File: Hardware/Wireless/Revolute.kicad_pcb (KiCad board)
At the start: 4 copper layers, 19.8 x 20 mm, 60 parts, among them U1 BQ27441-G1, U10 Button, U2 nrf52833_qfn40, U3 AS5600, U4 AP2112K-3.3, U5 BQ24075RGT, U6 Button, U8 Button, U9 Button, X1 32.768 kHz, X2 32MHZ

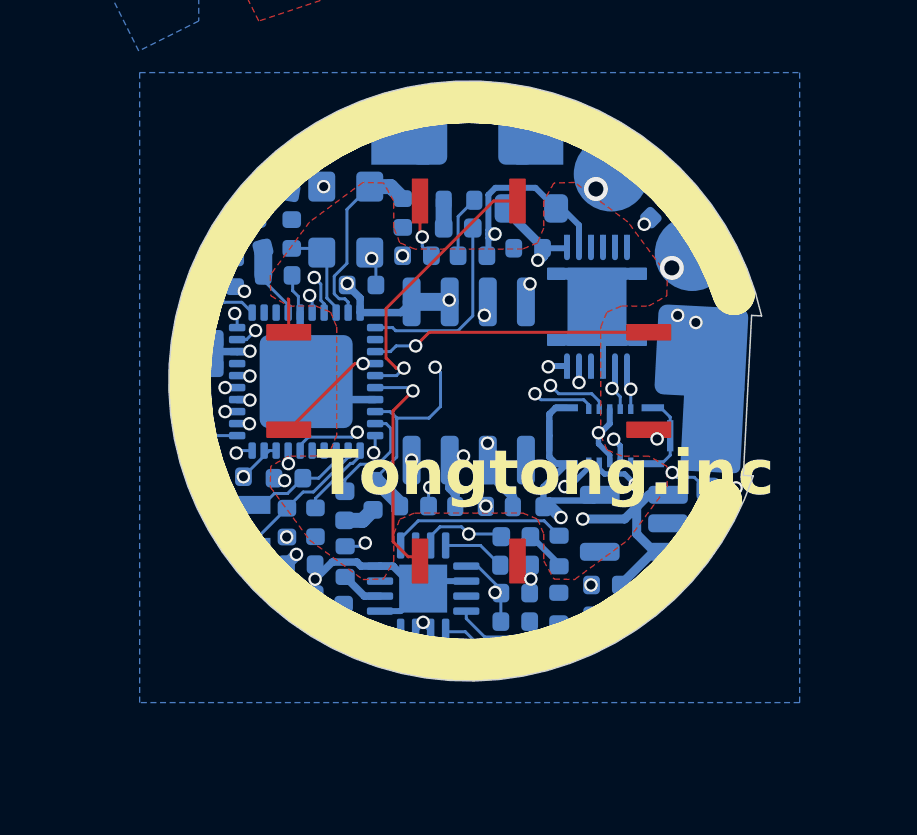
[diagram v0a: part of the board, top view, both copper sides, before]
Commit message: added testing pads to depricate fpc connector
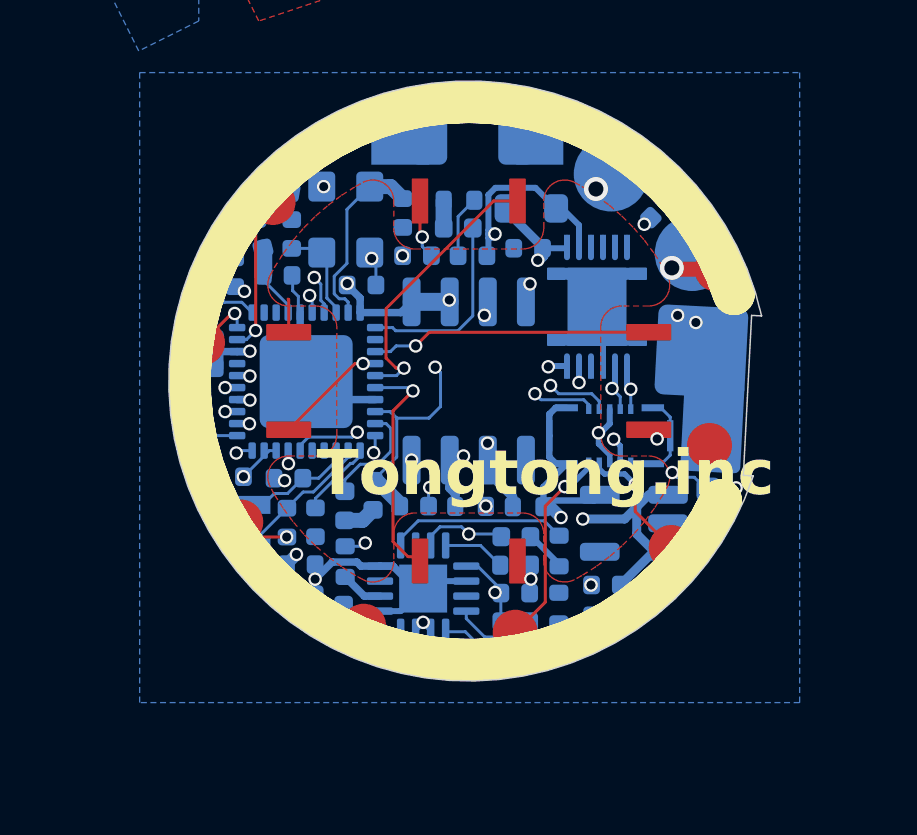
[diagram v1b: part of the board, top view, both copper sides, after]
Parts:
- added ?: , , F.Cu at (179.0, 97.2)
- added ?: , , F.Cu at (172.6, 103.4)
- added ?: , , F.Cu at (164.5, 89.0)
- added ?: , , F.Cu at (179.3, 91.3)
- added ?: , , F.Cu at (163.4, 99.7)
- added ?: , , F.Cu at (177.8, 100.5)
- added ?: , , F.Cu at (162.1, 93.7)
- added ?: , , F.Cu at (167.5, 103.2)
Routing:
- net D-: track 13.3 -> 18.9 mm
- net swd: track 13.8 -> 18.3 mm
- net D+: track 16.9 -> 19.4 mm
- net GND: track 35.4 -> 37.1 mm
- net VBUS: track 35.3 -> 36.8 mm
- net swc: track 15.5 -> 17.0 mm
- net VDD_nRF: track 22.3 -> 23.7 mm, vias 8 -> 9

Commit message: added ID column
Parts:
- AE1: value Antenna -> 2.4G ANT
- C12: value 0.47uF -> 470nF
- U7: value ~ -> BK13C06-10DS

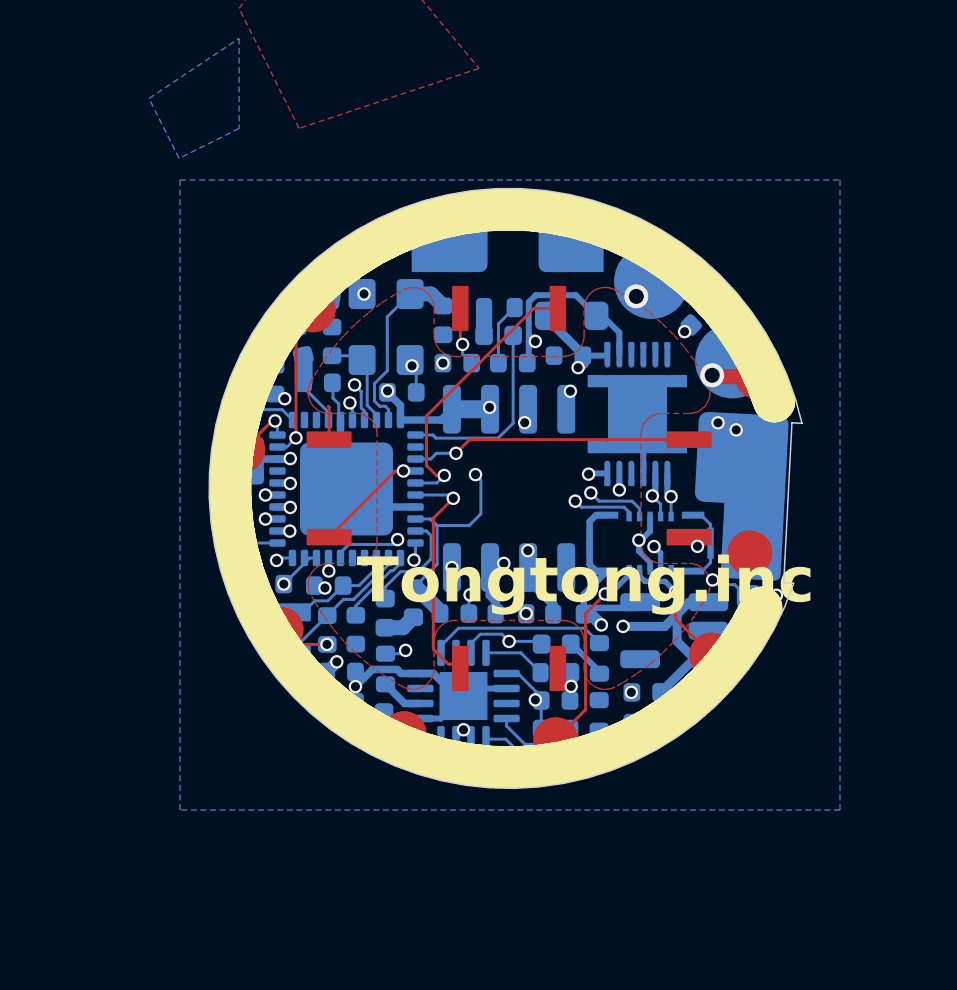
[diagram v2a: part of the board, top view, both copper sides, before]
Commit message: migrated components to 0201
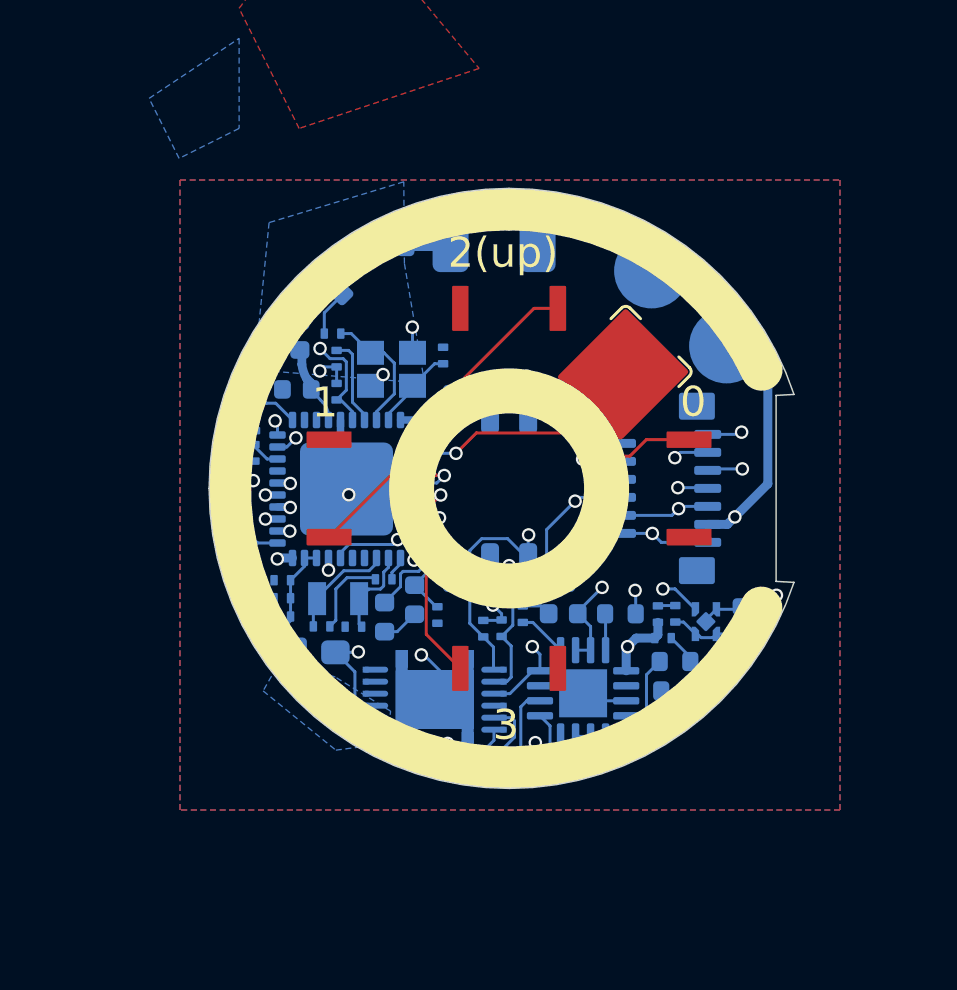
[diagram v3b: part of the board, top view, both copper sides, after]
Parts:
- removed ? (x11): , 
- removed C10: 100nF, Capacitor_SMD:C_0402_1005Metric
- added R10: 0Ω, Library:Resistor-0201, B.Cu at (171.1, 104.4)
- added REF**: Battery Base, Library:Battery Base, F.Cu at (171.0, 95.0)
- C1, C11, C12, C13, C14, C16, C17, C18, C2, C20, C21, C22, C23, C24, C3, C4, C5, C6, C7, C8, C9: footprint Capacitor_SMD:C_0402_1005Metric -> Library:Capacitor-0201
- R3: footprint Library:Resistor_0402_1005M-nosilk -> Library:Resistor-0201
- R6, R8: footprint Resistor_SMD:R_0402_1005Metric -> Library:Resistor-0201
- R7: value 10K -> 0Ω; footprint Library:Resistor_0402_1005M-nosilk -> Library:Resistor-0201
- R9: value 180 -> 1.5k; footprint Library:Resistor_0402_1005M-nosilk -> Library:Resistor-0201
- U4: value AP2112K-3.3 -> MIC5504; footprint Package_TO_SOT_SMD:SOT-23-5 -> Library:TDFN-4
- U7: value BK13C06-10DS -> Conn_01x14_Socket; footprint Library:BK13C06-10DS -> Library:FPC
- X2: footprint Library:crystal 32mhz -> Library:Crystal_SMD_2016-4Pin_2.0x1.6mm
- moved C12 16.9 mm to (169.9, 104.3), turned to 180 degrees
- moved R1 14.4 mm to (165.2, 101.3), turned to 90 degrees
- moved C25 13.6 mm to (163.9, 100.7), turned to -90 degrees
- moved C4 13.6 mm to (168.8, 104.2)
- moved R2 12.2 mm to (162.3, 97.9), turned to 90 degrees
- moved U1 11.7 mm to (168.5, 102.0), turned to 180 degrees
- moved D1 10.2 mm to (162.0, 95.4), turned to 90 degrees
- moved R7 6.16 mm to (172.1, 104.3), turned to 0 degrees
- moved C23 5.61 mm to (161.9, 92.8), turned to 90 degrees
- moved C24 5.13 mm to (176.0, 99.2), turned to 90 degrees
- moved C26 4.66 mm to (178.8, 99.4), turned to 90 degrees
- moved TH1 4.59 mm to (176.6, 101.8)
- moved C6 4.14 mm to (176.1, 100.0)
- moved C18 4.03 mm to (165.2, 90.7), turned to 90 degrees
- moved U5 3.99 mm to (173.5, 101.8)
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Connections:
- R7 pad 1: OUT -> GND
- R7 pad 2: Net-(U5-EN1) -> Net-(U5-EN2)
- U4 pad 1: OUT -> VDD_nRF
- U4 pad 4: unconnected-(U4-NC-Pad4) -> OUT
- U4 pad 5: VDD_nRF -> GND
- U5 pad 5: GND -> Net-(U5-EN2)
- U7 pad 1: swd -> swc
- U7 pad 11: VDD_nRF -> VBUS
- U7 pad 12: VDD_nRF -> Batteryin
- U7 pad 13: VDD_nRF -> Batteryin
- U7 pad 14: GND -> unconnected-(U7-Pin_14-Pad14)
- U7 pad 15: GND -> (no net)
- U7 pad 2: swc -> swd
- U7 pad 3: VBUS -> D-
- U7 pad 4: P0.15 -> D+
- U7 pad 5: P0.17 -> RESET
- U7 pad 6: D- -> VDD_nRF
- U7 pad 7: D+ -> P0.17
- U7 pad 8: VBUS -> P0.15
- U7 pad 9: RESET -> GND
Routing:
- net vBAT: track 21.5 -> 2.38 mm
- net Batteryin: track 22.5 -> 9.22 mm, vias 4 -> 3
- net VDD_nRF: track 23.7 -> 13.5 mm, vias 9 -> 7
- net ASOUT: track 9.98 -> 18.8 mm
- net OUT: track 20.5 -> 11.8 mm, vias 3 -> 2
- net VBUS: track 36.8 -> 29.5 mm, vias 4 -> 3
- net swd: track 18.3 -> 12.0 mm
- net GND: track 37.1 -> 31.1 mm, vias 24 -> 14
- net D+: track 19.4 -> 13.8 mm
- net 1.8V: track 8.23 -> 2.70 mm, vias 2 -> 0
- net P0.17: track 21.0 -> 26.3 mm
- net Net-(U5-~{CHG}): track 5.97 -> 1.64 mm
- net Net-(C19-Pad2): track 0.00 -> 3.87 mm
- net Net-(U2-XC2): track 6.26 -> 2.80 mm
- net D-: track 18.9 -> 15.6 mm
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- added copper zone on B.Cu, net vBAT
- added copper zone on In2.Cu, net vBAT
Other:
- board size 19.8 x 20 mm -> 19.5 x 20 mm
- board text added: "0"
- board text added: "1"
- board text added: "2(up)"
- board text added: "3"
- board text added: "Stack up JLC04161H-7628"

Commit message: refined pcb
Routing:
- added copper zone on B.Cu, net VBUS
- added copper zone on B.Cu, net VDD_nRF

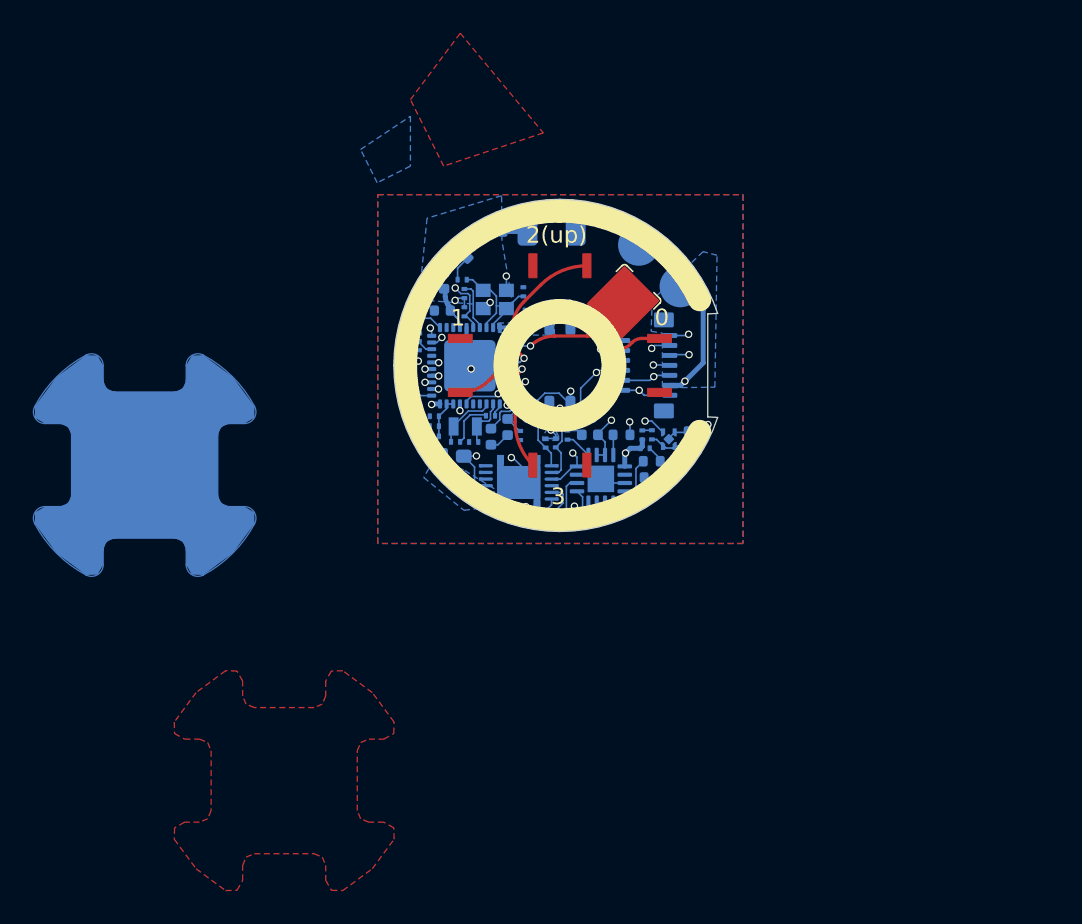
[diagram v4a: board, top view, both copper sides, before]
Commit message: updated pcb 0201 components and flex battery attachment
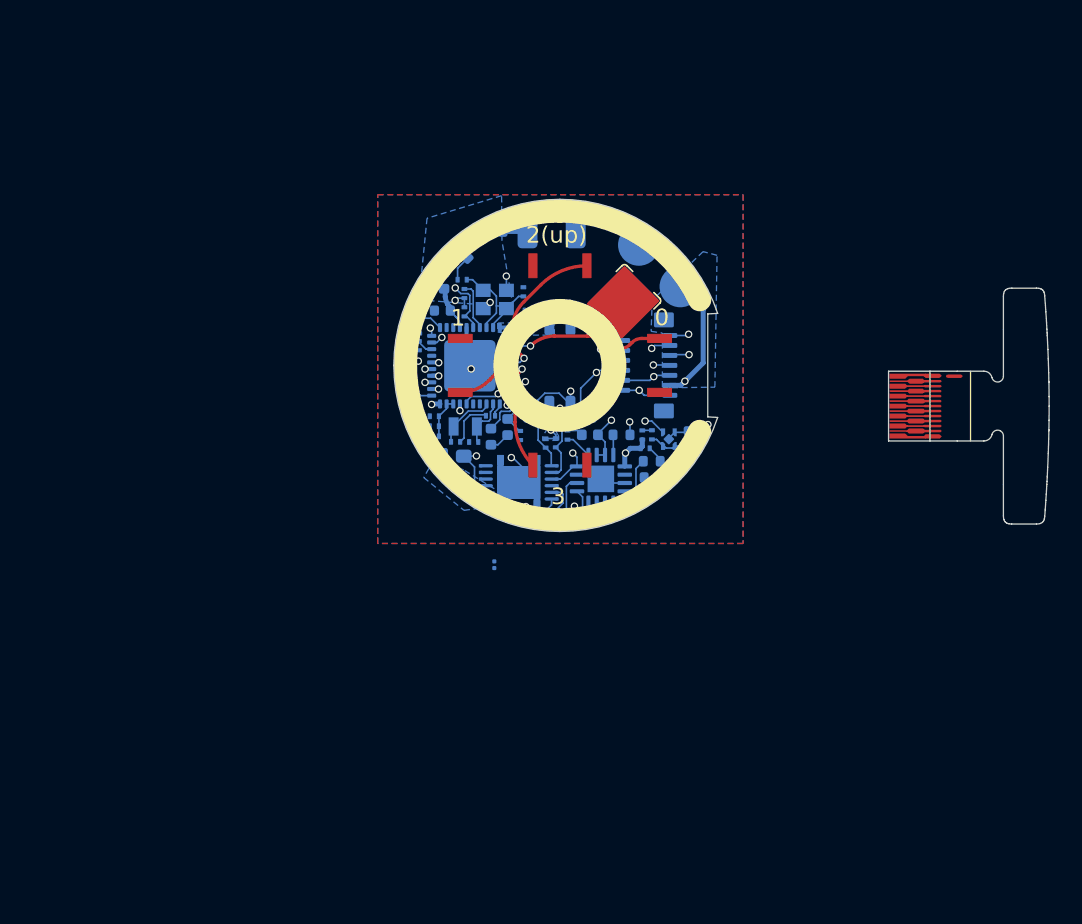
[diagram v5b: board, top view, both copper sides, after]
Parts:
- added REF**: C_01005_0402Metric, Capacitor_SMD:C_01005_0402Metric, B.Cu at (167.1, 107.0)
- added REF**: flex connector, Library:flex connector, B.Cu at (194.7, 95.2)
- moved AE1 0.16 mm to (170.5, 87.0)
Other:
- board size 19.5 x 20 mm -> 39.5 x 20 mm

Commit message: current version
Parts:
- removed the REF** at (167.1, 107.0)
- removed the REF** at (194.7, 95.2)
- AE1: footprint RF_Antenna:Johanson_2450AT18x100 -> Library:Antenna 2450AT42A100
- C15, C19: footprint Capacitor_SMD:C_0402_1005Metric -> Library:Capacitor-0201
- R2: footprint Library:Resistor_0402_1005M-nosilk -> Library:Resistor-0201
- moved L4 3.34 mm to (164.5, 89.1), turned to 30 degrees
- moved C19 2.39 mm to (163.6, 90.0), turned to 130 degrees
- moved AE1 2.29 mm to (168.5, 88.2), turned to 18 degrees
- moved R2 1.21 mm to (162.0, 96.7), turned to 0 degrees
- moved L3 1.20 mm to (163.3, 90.8), turned to 130 degrees
- moved C8 1.14 mm to (162.5, 97.7), turned to 90 degrees
- moved C14 0.46 mm to (162.4, 92.0), turned to 0 degrees
- moved C15 0.32 mm to (164.2, 91.8), turned to 45 degrees
- moved C9 0.08 mm to (165.2, 91.7)
- moved C25 0.07 mm to (164.0, 100.8)
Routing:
- net GND: track 31.1 -> 38.7 mm, vias 14 -> 17
- net Net-(C19-Pad2): track 3.87 -> 1.64 mm
- net OUT: track 11.8 -> 10.5 mm
- net Net-(U2-DEC4): track 15.7 -> 17.0 mm
- net P0.15: track 23.3 -> 22.3 mm
- net vBAT: track 2.38 -> 1.50 mm
- net Net-(D1-K): track 1.62 -> 0.90 mm
- net Batteryin: track 9.22 -> 9.82 mm
- net P0.17: track 26.3 -> 25.7 mm
- net RESET: track 18.1 -> 17.6 mm
- net VBUS: track 29.5 -> 29.4 mm, vias 3 -> 7
- added copper zone on B.Cu, net OUT
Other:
- board size 39.5 x 20 mm -> 19.5 x 20 mm
